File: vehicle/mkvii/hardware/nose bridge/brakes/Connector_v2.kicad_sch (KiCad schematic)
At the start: 2 parts, among them J1 CONN_pcie_x1

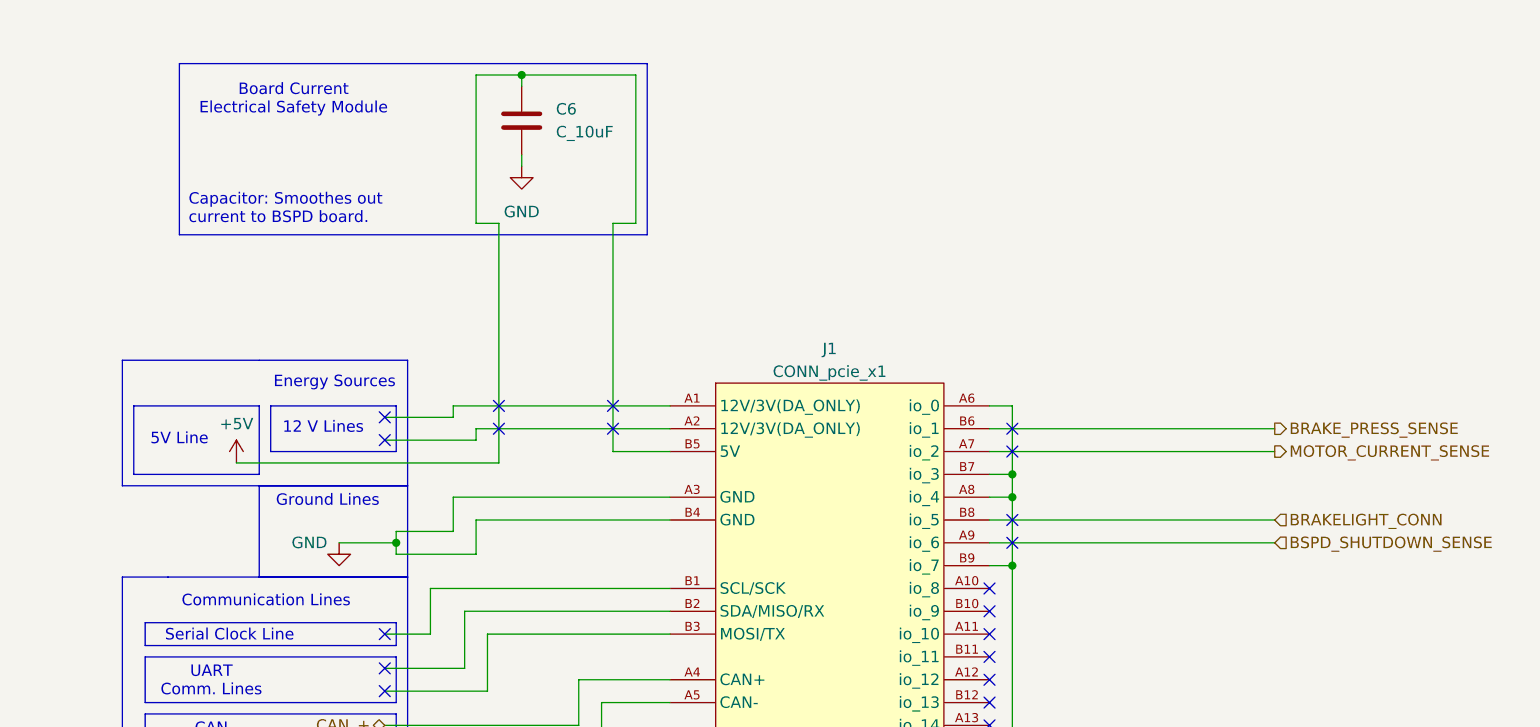
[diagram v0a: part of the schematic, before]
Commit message: BSPD Schmatics Update v2 (with 10-22-2024 revisions from Ian Walsh)
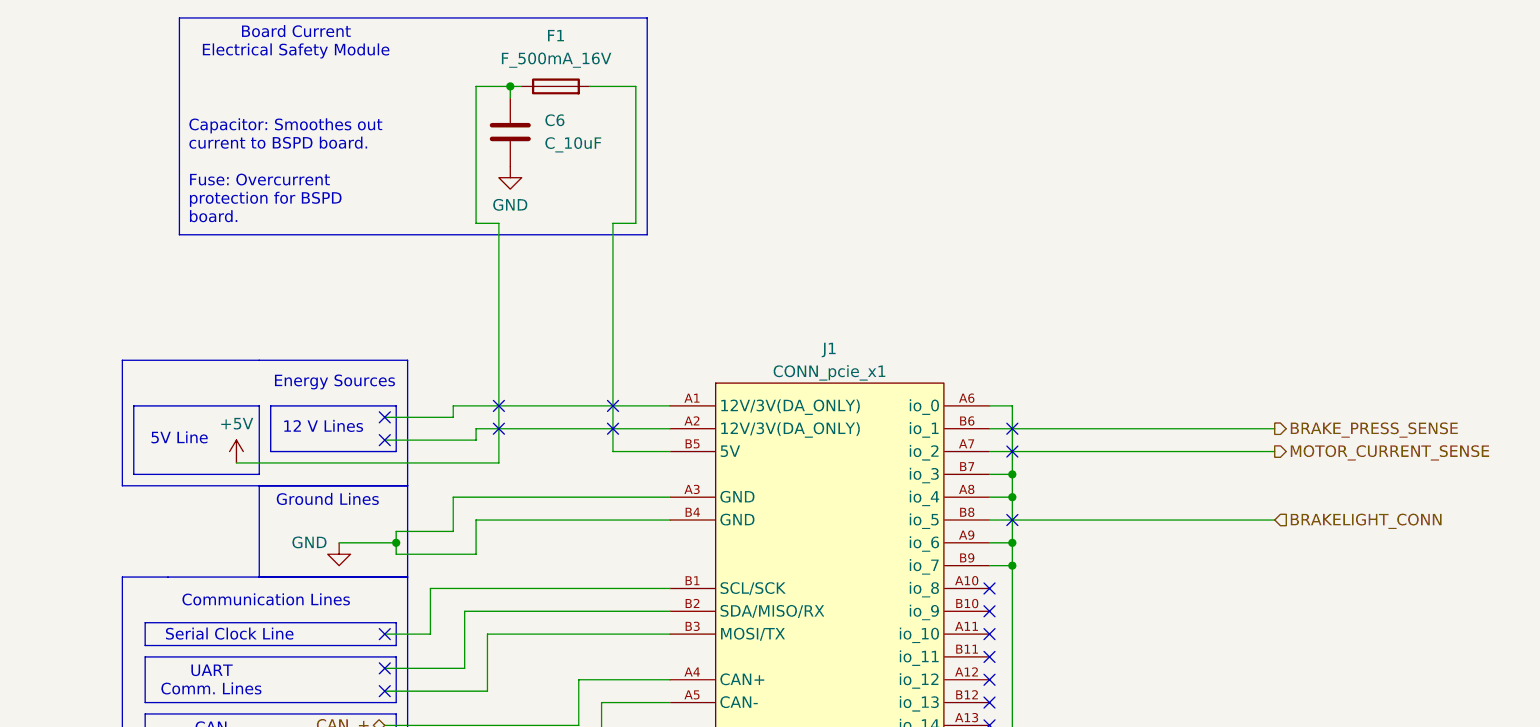
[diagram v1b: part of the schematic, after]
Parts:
- added F1: F_500mA_16V, OEM:Fuse_1210, symbol OEM:F_500mA_16V
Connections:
- net BSPD_SHUTDOWN_SENSE is gone; now on net GND: J1.A9 (io_6)
- net +5V: now also F1.1; no longer J1.B5 (5V)
- new net: F1.2, J1.B5 (5V)
- no-connect marks 27 -> 26
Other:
- note added: "Capacitor: Smoothes out current to BSPD board. Fuse: Overcurrent protection for BSPD board."
- note removed: "Capacitor: Smoothes out current to BSPD board."
- moved on the sheet: C6

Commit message: Final BSPD PCB Layout (without Bean Logo)
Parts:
- added H1: CONN_MountingHole, OEM:PCIe_Mount, symbol OEM:CONN_MountingHole
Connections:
- net GND: now also H1.1
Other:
- note added: "PCIe x1 Mounting Hole"
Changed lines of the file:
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@@
+		)
+	)
+	(polyline
+		(pts
+			(xy 205.74 52.07) (xy 205.74 27.94)
+		)
+		(stroke
+			(width 0)
+			(type default)
 		)
 	)
@@
 		)
 	)
+	(polyline
+		(pts
+			(xy 165.1 27.94) (xy 205.74 27.94)
+		)
+		(stroke
+			(width 0)
+			(type default)
+		)
+	)
 	(wire
 		(pts
@@
 	(polyline
 		(pts
+			(xy 165.1 52.07) (xy 205.74 52.07)
+		)
+		(stroke
+			(width 0)
+			(type default)
+		)
+	)
+	(polyline
+		(pts
 			(xy 95.25 128.27) (xy 124.46 128.27)
 		)
@@
 		(pts
 			(xy 146.05 104.14) (xy 153.67 104.14)
+		)
+		(stroke
+			(width 0)
+			(type default)
+		)
+	)
+	(polyline
+		(pts
+			(xy 165.1 27.94) (xy 165.1 52.07)
 		)
 		(stroke
@@
 		(exclude_from_sim no)
 		(at 99.06 74.93 0)
+		(effects
+			(font
+				(size 1.27 1.27)
+			)
+		)
+	)
+	(text "PCIe x1 Mounting Hole"
+		(exclude_from_sim no)
+		(at 185.674 31.242 0)
 		(effects
 			(font
@@
 	)
 	(symbol
+		(lib_id "OEM:CONN_MountingHole")
+		(at 177.8 39.37 0)
+		(unit 1)
+		(exclude_from_sim no)
+		(in_bom no)
+		(on_board yes)
+		(dnp no)
+		(property "Reference" "H1"
+			(at 180.34 36.8299 0)
+			(effects
+				(font
+					(size 1.27 1.27)
+				)
+				(justify left)
+			)
+		)
+		(property "Value" "CONN_MountingHole"
+			(at 180.34 39.3699 0)
+			(effects
+				(font
+					(size 1.27 1.27)
+				)
+				(justify left)
+			)
+		)
+		(property "Footprint" "OEM:PCIe_Mount"
+			(at 177.8 39.37 0)
+			(effects
+				(font
+					(size 1.27 1.27)
+				)
+				(hide yes)
+			)
+		)
+		(property "Datasheet" "~"
+			(at 177.8 39.37 0)
+			(effects
+				(font
+					(size 1.27 1.27)
+				)
+				(hide yes)
+			)
+		)
+		(property "Description" "Mounting Hole with connection"
+			(at 177.8 39.37 0)
+			(effects
+				(font
+					(size 1.27 1.27)
+				)
+				(hide yes)
+			)
+		)
+		(pin "1"
+		)
+		(instances
+			(project ""
+				(path "/10f522c8-3a01-4239-b7df-a730ca32b367/875aabfb-3c91-4011-8240-4af05d59512e"
+					(reference "H1")
+					(unit 1)
+				)
+			)
+		)
+	)
+	(symbol
 		(lib_id "power:GND")
 		(at 116.84 86.36 0)
@@
 					(unit 1)
 				)
+			)
+		)
+	)
+	(symbol
+		(lib_id "power:GND")
+		(at 177.8 41.91 0)
+		(unit 1)
+		(exclude_from_sim no)
+		(in_bom yes)
+		(on_board yes)
+		(dnp no)
+		(fields_autoplaced yes)
+		(property "Reference" "#PWR?"
+			(at 177.8 48.26 0)
+			(effects
+				(font
+					(size 1.27 1.27)
+				)
+				(hide yes)
+			)
+		)
+		(property "Value" "GND"
+			(at 177.8 46.99 0)
+			(effects
+				(font
+					(size 1.27 1.27)
+				)
+			)
+		)
+		(property "Footprint" ""
+			(at 177.8 41.91 0)
+			(effects
+				(font
+					(size 1.27 1.27)
+				)
+				(hide yes)
+			)
+		)
+		(property "Datasheet" ""
+			(at 177.8 41.91 0)
+			(effects
+				(font
+					(size 1.27 1.27)
+				)
+				(hide yes)
+			)
+		)
+		(property "Description" "Power symbol creates a global label with name \"GND\" , ground"
+			(at 177.8 41.91 0)
+			(effects
+				(font
+					(size 1.27 1.27)
+				)
+				(hide yes)
+			)
+		)
+		(pin "1"
+		)
+		(instances
+			(project ""
+				(path "/10f522c8-3a01-4239-b7df-a730ca32b367/875aabfb-3c91-4011-8240-4af05d59512e"
+					(reference "#PWR?")
+					(unit 1)
+				)
